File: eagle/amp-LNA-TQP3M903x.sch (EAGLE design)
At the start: 17 parts, among them J1 142-0701-851, J2 142-0701-851, U1 TQP3M903X

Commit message: Tune S band
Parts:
- added C7: 2.4p, oresat-rcl:C-EU0402-C-NOSILK
- added L2: 2.7n, oresat-rcl:L-US0402-C-NOSILK
- C5, C6: value ? -> 100p
- L1: value ? -> 4.3n
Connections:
- net RF_IN renamed N$6
- removed net N$32: C5.2, U1.IN
- new net N$4: C7.2, U1.IN
- new net N$5: C5.2, C7.1, L2.1
- net GND: now also L2.2
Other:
- note added: "L band - 1265MHz: L1 = ? L2 = ? C7 = ? Notes: C7 @ ? deg distance"
- note added: "S band - 2422MHz: L1 = 4.3n L2 = 2.7n C7 = 2.4p Notes: C7 @ 12 deg distance"
- note added: "UHF - 436.5MHz: L1 = ? L2 = ? C7 = ? Notes: C7 @ ? deg distance"
- note removed: "Allow for shunt"
- note removed: "Allow for shunt L"
- note removed: "Note: LC input/output networks require tuning"
- note removed: "UHF / L band / S band"
- moved on the sheet: C5, C6, J1
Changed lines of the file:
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@@
 </class>
 <class number="1" name="RF1" width="0" drill="0">
-<clearance class="1" value="0.4"/>
+<clearance class="1" value="0.5"/>
 </class>
 <class number="2" name="RF2" width="0" drill="0">
-<clearance class="2" value="0.6"/>
+<clearance class="2" value="0.4"/>
 </class>
 </classes>
@@
 <part name="GND27" library="supply1" library_urn="urn:adsk.eagle:library:371" deviceset="GND" device=""/>
 <part name="GND28" library="supply1" library_urn="urn:adsk.eagle:library:371" deviceset="GND" device=""/>
-<part name="C6" library="oresat-rcl" deviceset="C-EU" device="0402-C-NOSILK" value="?"/>
-<part name="C5" library="oresat-rcl" deviceset="C-EU" device="0402-C-NOSILK" value="?"/>
+<part name="C6" library="oresat-rcl" deviceset="C-EU" device="0402-C-NOSILK" value="100p"/>
+<part name="C5" library="oresat-rcl" deviceset="C-EU" device="0402-C-NOSILK" value="100p"/>
 <part name="GND29" library="supply1" library_urn="urn:adsk.eagle:library:371" deviceset="GND" device=""/>
 <part name="GND30" library="supply1" library_urn="urn:adsk.eagle:library:371" deviceset="GND" device=""/>
@@
 <part name="R5" library="oresat-rcl" deviceset="R-US_" device="0603-B-NOSILK" value="10k"/>
 <part name="GND3" library="supply1" library_urn="urn:adsk.eagle:library:371" deviceset="GND" device=""/>
-<part name="L1" library="oresat-rcl" deviceset="L-US" device="0603-C-NOSILK" value="?"/>
+<part name="L1" library="oresat-rcl" deviceset="L-US" device="0603-C-NOSILK" value="4.3n"/>
+<part name="C7" library="oresat-rcl" deviceset="C-EU" device="0402-C-NOSILK" value="2.4p"/>
+<part name="L2" library="oresat-rcl" deviceset="L-US" device="0402-C-NOSILK" value="2.7n"/>
+<part name="GND2" library="supply1" library_urn="urn:adsk.eagle:library:371" deviceset="GND" device=""/>
 </parts>
 <sheets>
@@
 <text x="176.53" y="26.67" size="5.08" layer="94">LNA: Qorvo TQP3M9035/6/7</text>
 <text x="265.43" y="6.35" size="3.81" layer="94">1</text>
-<text x="162.56" y="86.36" size="1.778" layer="97">Note: LC input/output networks require tuning</text>
 <text x="170.18" y="137.16" size="1.778" layer="97">Bias Resistor NOT Required</text>
-<text x="163.83" y="68.58" size="1.778" layer="97">UHF / L band / S band</text>
+<text x="173.99" y="81.28" size="1.778" layer="97" rot="MR180">S band - 2422MHz:
+L1 = 4.3n
+L2 = 2.7n
+C7 = 2.4p
+Notes:
+C7 @ 12 deg distance</text>
 <text x="95.25" y="74.93" size="1.778" layer="97">Shutdown (High)
 Enable (Low - Default)</text>
@@
 External</text>
 <text x="121.92" y="110.49" size="1.778" layer="97">Pad for input bias</text>
-<text x="102.87" y="99.06" size="1.778" layer="97">Allow for shunt L</text>
-<text x="182.88" y="99.06" size="1.778" layer="97">Allow for shunt</text>
+<text x="208.28" y="81.28" size="1.778" layer="97" rot="MR180">L band - 1265MHz:
+L1 = ?
+L2 = ?
+C7 = ?
+Notes:
+C7 @ ? deg distance</text>
+<text x="241.3" y="81.28" size="1.778" layer="97" rot="MR180">UHF - 436.5MHz:
+L1 = ?
+L2 = ?
+C7 = ?
+Notes:
+C7 @ ? deg distance</text>
 </plain>
 <instances>
@@
 <attribute name="VALUE" x="157.48" y="82.55" size="1.778" layer="96" rot="MR0"/>
 </instance>
-<instance part="C6" gate="CE" x="173.99" y="104.14" smashed="yes" rot="MR270">
-<attribute name="NAME" x="173.609" y="102.616" size="1.778" layer="95" rot="MR270"/>
-<attribute name="VALUE" x="178.689" y="102.616" size="1.778" layer="96" rot="MR270"/>
-</instance>
-<instance part="C5" gate="CE" x="119.38" y="104.14" smashed="yes" rot="R90">
-<attribute name="NAME" x="118.999" y="105.664" size="1.778" layer="95" rot="R90"/>
-<attribute name="VALUE" x="124.079" y="105.664" size="1.778" layer="96" rot="R90"/>
+<instance part="C6" gate="CE" x="182.88" y="104.14" smashed="yes" rot="MR270">
+<attribute name="NAME" x="182.499" y="102.616" size="1.778" layer="95" rot="MR270"/>
+<attribute name="VALUE" x="187.579" y="102.616" size="1.778" layer="96" rot="MR270"/>
+</instance>
+<instance part="C5" gate="CE" x="101.6" y="104.14" smashed="yes" rot="R90">
+<attribute name="NAME" x="101.219" y="105.664" size="1.778" layer="95" rot="R90"/>
+<attribute name="VALUE" x="106.299" y="105.664" size="1.778" layer="96" rot="R90"/>
 </instance>
 <instance part="GND29" gate="1" x="201.93" y="96.52" smashed="yes">
 <attribute name="VALUE" x="199.39" y="93.98" size="1.778" layer="96"/>
 </instance>
-<instance part="GND30" gate="1" x="99.06" y="96.52" smashed="yes" rot="MR0">
-<attribute name="VALUE" x="101.6" y="93.98" size="1.778" layer="96" rot="MR0"/>
+<instance part="GND30" gate="1" x="93.98" y="96.52" smashed="yes" rot="MR0">
+<attribute name="VALUE" x="96.52" y="93.98" size="1.778" layer="96" rot="MR0"/>
 </instance>
 <instance part="GND81" gate="1" x="200.66" y="114.3" smashed="yes">
@@
 <attribute name="VALUE" x="156.21" y="151.638" size="1.778" layer="96"/>
 </instance>
-<instance part="J1" gate="G$1" x="93.98" y="104.14" smashed="yes">
-<attribute name="NAME" x="91.44" y="99.06" size="1.778" layer="95"/>
-<attribute name="VALUE" x="85.09" y="106.68" size="1.778" layer="96"/>
+<instance part="J1" gate="G$1" x="88.9" y="104.14" smashed="yes">
+<attribute name="NAME" x="86.36" y="99.06" size="1.778" layer="95"/>
+<attribute name="VALUE" x="80.01" y="106.68" size="1.778" layer="96"/>
 </instance>
 <instance part="J2" gate="G$1" x="207.01" y="104.14" smashed="yes" rot="MR0">
@@
 <attribute name="NAME" x="163.83" y="116.84" size="1.778" layer="95"/>
 <attribute name="VALUE" x="168.91" y="116.84" size="1.778" layer="96"/>
+</instance>
+<instance part="C7" gate="CE" x="121.92" y="104.14" smashed="yes" rot="MR270">
+<attribute name="NAME" x="121.539" y="102.616" size="1.778" layer="95" rot="MR270"/>
+<attribute name="VALUE" x="126.619" y="102.616" size="1.778" layer="96" rot="MR270"/>
+</instance>
+<instance part="L2" gate="L" x="114.3" y="92.71" smashed="yes" rot="R270">
+<attribute name="NAME" x="110.49" y="93.98" size="1.778" layer="95"/>
+<attribute name="VALUE" x="115.57" y="93.98" size="1.778" layer="96"/>
+</instance>
+<instance part="GND2" gate="1" x="114.3" y="85.09" smashed="yes" rot="MR0">
+<attribute name="VALUE" x="116.84" y="82.55" size="1.778" layer="96" rot="MR0"/>
 </instance>
 </instances>
@@
 </segment>
 <segment>
-<wire x1="99.06" y1="101.6" x2="96.52" y2="101.6" width="0.1524" layer="91"/>
+<wire x1="93.98" y1="101.6" x2="91.44" y2="101.6" width="0.1524" layer="91"/>
 <pinref part="GND30" gate="1" pin="GND"/>
-<wire x1="99.06" y1="99.06" x2="99.06" y2="101.6" width="0.1524" layer="91"/>
+<wire x1="93.98" y1="99.06" x2="93.98" y2="101.6" width="0.1524" layer="91"/>
 <pinref part="J1" gate="G$1" pin="GND"/>
 </segment>
@@
 <wire x1="149.86" y1="71.12" x2="149.86" y2="69.85" width="0.1524" layer="91"/>
 </segment>
+<segment>
+<pinref part="L2" gate="L" pin="2"/>
+<pinref part="GND2" gate="1" pin="GND"/>
+</segment>
 </net>
 <net name="N$28" class="1">
@@
 <wire x1="167.64" y1="104.14" x2="167.64" y2="110.49" width="0.1524" layer="91"/>
 <pinref part="C6" gate="CE" pin="1"/>
-<wire x1="171.45" y1="104.14" x2="167.64" y2="104.14" width="0.1524" layer="91"/>
+<wire x1="180.34" y1="104.14" x2="167.64" y2="104.14" width="0.1524" layer="91"/>
 <junction x="167.64" y="104.14"/>
 <pinref part="L1" gate="L" pin="2"/>
 </segment>
 </net>
-<net name="N$32" class="1">
-<segment>
-<pinref part="C5" gate="CE" pin="2"/>
-<pinref part="U1" gate="G$1" pin="IN"/>
-<wire x1="124.46" y1="104.14" x2="137.16" y2="104.14" width="0.1524" layer="91"/>
-</segment>
-</net>
-<net name="RF_OUT" class="2">
+<net name="RF_OUT" class="1">
 <segment>
 <wire x1="199.39" y1="104.14" x2="204.47" y2="104.14" width="0.1524" layer="91"/>
 <pinref part="C6" gate="CE" pin="2"/>
-<wire x1="199.39" y1="104.14" x2="179.07" y2="104.14" width="0.1524" layer="91"/>
+<wire x1="199.39" y1="104.14" x2="187.96" y2="104.14" width="0.1524" layer="91"/>
 <pinref part="J2" gate="G$1" pin="RF"/>
-</segment>
-</net>
-<net name="RF_IN" class="2">
-<segment>
-<wire x1="101.6" y1="104.14" x2="96.52" y2="104.14" width="0.1524" layer="91"/>
-<wire x1="101.6" y1="104.14" x2="106.68" y2="104.14" width="0.1524" layer="91"/>
-<pinref part="C5" gate="CE" pin="1"/>
-<pinref part="J1" gate="G$1" pin="RF"/>
-<wire x1="106.68" y1="104.14" x2="116.84" y2="104.14" width="0.1524" layer="91"/>
 </segment>
 </net>
@@
 </segment>
 </net>
+<net name="N$4" class="1">
+<segment>
+<pinref part="C7" gate="CE" pin="2"/>
+<pinref part="U1" gate="G$1" pin="IN"/>
+<wire x1="127" y1="104.14" x2="137.16" y2="104.14" width="0.1524" layer="91"/>
+</segment>
+</net>
+<net name="N$5" class="1">
+<segment>
+<pinref part="C7" gate="CE" pin="1"/>
+<pinref part="C5" gate="CE" pin="2"/>
+<wire x1="119.38" y1="104.14" x2="114.3" y2="104.14" width="0.1524" layer="91"/>
+<pinref part="L2" gate="L" pin="1"/>
+<wire x1="114.3" y1="104.14" x2="106.68" y2="104.14" width="0.1524" layer="91"/>
+<wire x1="114.3" y1="100.33" x2="114.3" y2="104.14" width="0.1524" layer="91"/>
+<junction x="114.3" y="104.14"/>
+</segment>
+</net>
+<net name="N$6" class="1">
+<segment>
+<pinref part="C5" gate="CE" pin="1"/>
+<pinref part="J1" gate="G$1" pin="RF"/>
+<wire x1="99.06" y1="104.14" x2="91.44" y2="104.14" width="0.1524" layer="91"/>
+</segment>
+</net>

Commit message: Minor fixes
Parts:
- removed C7: 2.4p, oresat-rcl:C-EU0402-C-NOSILK
- C5: value 100p -> 2.4p
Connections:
- removed net N$5: C5.2, C7.1, L2.1
- removed net N$6: C5.1, J1.RF
- new net RF_IN: C5.1, J1.RF, L2.1
- net N$4: now also C5.2; no longer C7.2
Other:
- note added: "L band - 1265MHz: L1 = ? L2 = ? C7 = ? Notes: C5 @ ? deg distance"
- note added: "S band - 2422MHz: L1 = 4.3n L2 = 2.7n C7 = 2.4p Notes: C5 @ 12 deg distance Tuned for 3.3V"
- note added: "UHF - 436.5MHz: L1 = ? L2 = ? C7 = ? Notes: C5 @ ? deg distance"
- note removed: "L band - 1265MHz: L1 = ? L2 = ? C7 = ? Notes: C7 @ ? deg distance"
- note removed: "S band - 2422MHz: L1 = 4.3n L2 = 2.7n C7 = 2.4p Notes: C7 @ 12 deg distance"
- note removed: "UHF - 436.5MHz: L1 = ? L2 = ? C7 = ? Notes: C7 @ ? deg distance"
- moved on the sheet: C5
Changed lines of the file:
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@@
 </class>
 <class number="2" name="RF2" width="0" drill="0">
-<clearance class="2" value="0.4"/>
+<clearance class="2" value="0.8"/>
 </class>
 </classes>
@@
 <part name="GND28" library="supply1" library_urn="urn:adsk.eagle:library:371" deviceset="GND" device=""/>
 <part name="C6" library="oresat-rcl" deviceset="C-EU" device="0402-C-NOSILK" value="100p"/>
-<part name="C5" library="oresat-rcl" deviceset="C-EU" device="0402-C-NOSILK" value="100p"/>
 <part name="GND29" library="supply1" library_urn="urn:adsk.eagle:library:371" deviceset="GND" device=""/>
 <part name="GND30" library="supply1" library_urn="urn:adsk.eagle:library:371" deviceset="GND" device=""/>
@@
 <part name="GND3" library="supply1" library_urn="urn:adsk.eagle:library:371" deviceset="GND" device=""/>
 <part name="L1" library="oresat-rcl" deviceset="L-US" device="0603-C-NOSILK" value="4.3n"/>
-<part name="C7" library="oresat-rcl" deviceset="C-EU" device="0402-C-NOSILK" value="2.4p"/>
+<part name="C5" library="oresat-rcl" deviceset="C-EU" device="0402-C-NOSILK" value="2.4p"/>
 <part name="L2" library="oresat-rcl" deviceset="L-US" device="0402-C-NOSILK" value="2.7n"/>
 <part name="GND2" library="supply1" library_urn="urn:adsk.eagle:library:371" deviceset="GND" device=""/>
@@
 C7 = 2.4p
 Notes:
-C7 @ 12 deg distance</text>
+C5 @ 12 deg distance
+Tuned for 3.3V</text>
 <text x="95.25" y="74.93" size="1.778" layer="97">Shutdown (High)
 Enable (Low - Default)</text>
@@
 C7 = ?
 Notes:
-C7 @ ? deg distance</text>
+C5 @ ? deg distance</text>
 <text x="241.3" y="81.28" size="1.778" layer="97" rot="MR180">UHF - 436.5MHz:
 L1 = ?
@@
 C7 = ?
 Notes:
-C7 @ ? deg distance</text>
+C5 @ ? deg distance</text>
 </plain>
 <instances>
@@
 <attribute name="VALUE" x="187.579" y="102.616" size="1.778" layer="96" rot="MR270"/>
 </instance>
-<instance part="C5" gate="CE" x="101.6" y="104.14" smashed="yes" rot="R90">
-<attribute name="NAME" x="101.219" y="105.664" size="1.778" layer="95" rot="R90"/>
-<attribute name="VALUE" x="106.299" y="105.664" size="1.778" layer="96" rot="R90"/>
-</instance>
 <instance part="GND29" gate="1" x="201.93" y="96.52" smashed="yes">
 <attribute name="VALUE" x="199.39" y="93.98" size="1.778" layer="96"/>
@@
 <attribute name="VALUE" x="168.91" y="116.84" size="1.778" layer="96"/>
 </instance>
-<instance part="C7" gate="CE" x="121.92" y="104.14" smashed="yes" rot="MR270">
+<instance part="C5" gate="CE" x="121.92" y="104.14" smashed="yes" rot="MR270">
 <attribute name="NAME" x="121.539" y="102.616" size="1.778" layer="95" rot="MR270"/>
 <attribute name="VALUE" x="126.619" y="102.616" size="1.778" layer="96" rot="MR270"/>
@@
 </segment>
 </net>
-<net name="RF_OUT" class="1">
+<net name="RF_OUT" class="2">
 <segment>
 <wire x1="199.39" y1="104.14" x2="204.47" y2="104.14" width="0.1524" layer="91"/>
@@
 <net name="N$4" class="1">
 <segment>
-<pinref part="C7" gate="CE" pin="2"/>
+<pinref part="C5" gate="CE" pin="2"/>
 <pinref part="U1" gate="G$1" pin="IN"/>
 <wire x1="127" y1="104.14" x2="137.16" y2="104.14" width="0.1524" layer="91"/>
 </segment>
 </net>
-<net name="N$5" class="1">
-<segment>
-<pinref part="C7" gate="CE" pin="1"/>
-<pinref part="C5" gate="CE" pin="2"/>
+<net name="RF_IN" class="2">
+<segment>
+<pinref part="C5" gate="CE" pin="1"/>
 <wire x1="119.38" y1="104.14" x2="114.3" y2="104.14" width="0.1524" layer="91"/>
 <pinref part="L2" gate="L" pin="1"/>
-<wire x1="114.3" y1="104.14" x2="106.68" y2="104.14" width="0.1524" layer="91"/>
 <wire x1="114.3" y1="100.33" x2="114.3" y2="104.14" width="0.1524" layer="91"/>
+<pinref part="J1" gate="G$1" pin="RF"/>
+<wire x1="91.44" y1="104.14" x2="114.3" y2="104.14" width="0.1524" layer="91"/>
 <junction x="114.3" y="104.14"/>
-</segment>
-</net>
-<net name="N$6" class="1">
-<segment>
-<pinref part="C5" gate="CE" pin="1"/>
-<pinref part="J1" gate="G$1" pin="RF"/>
-<wire x1="99.06" y1="104.14" x2="91.44" y2="104.14" width="0.1524" layer="91"/>
 </segment>
 </net>
@@
 </sheet>
 </sheets>
+<errors>
+</errors>
 </schematic>
 </drawing>

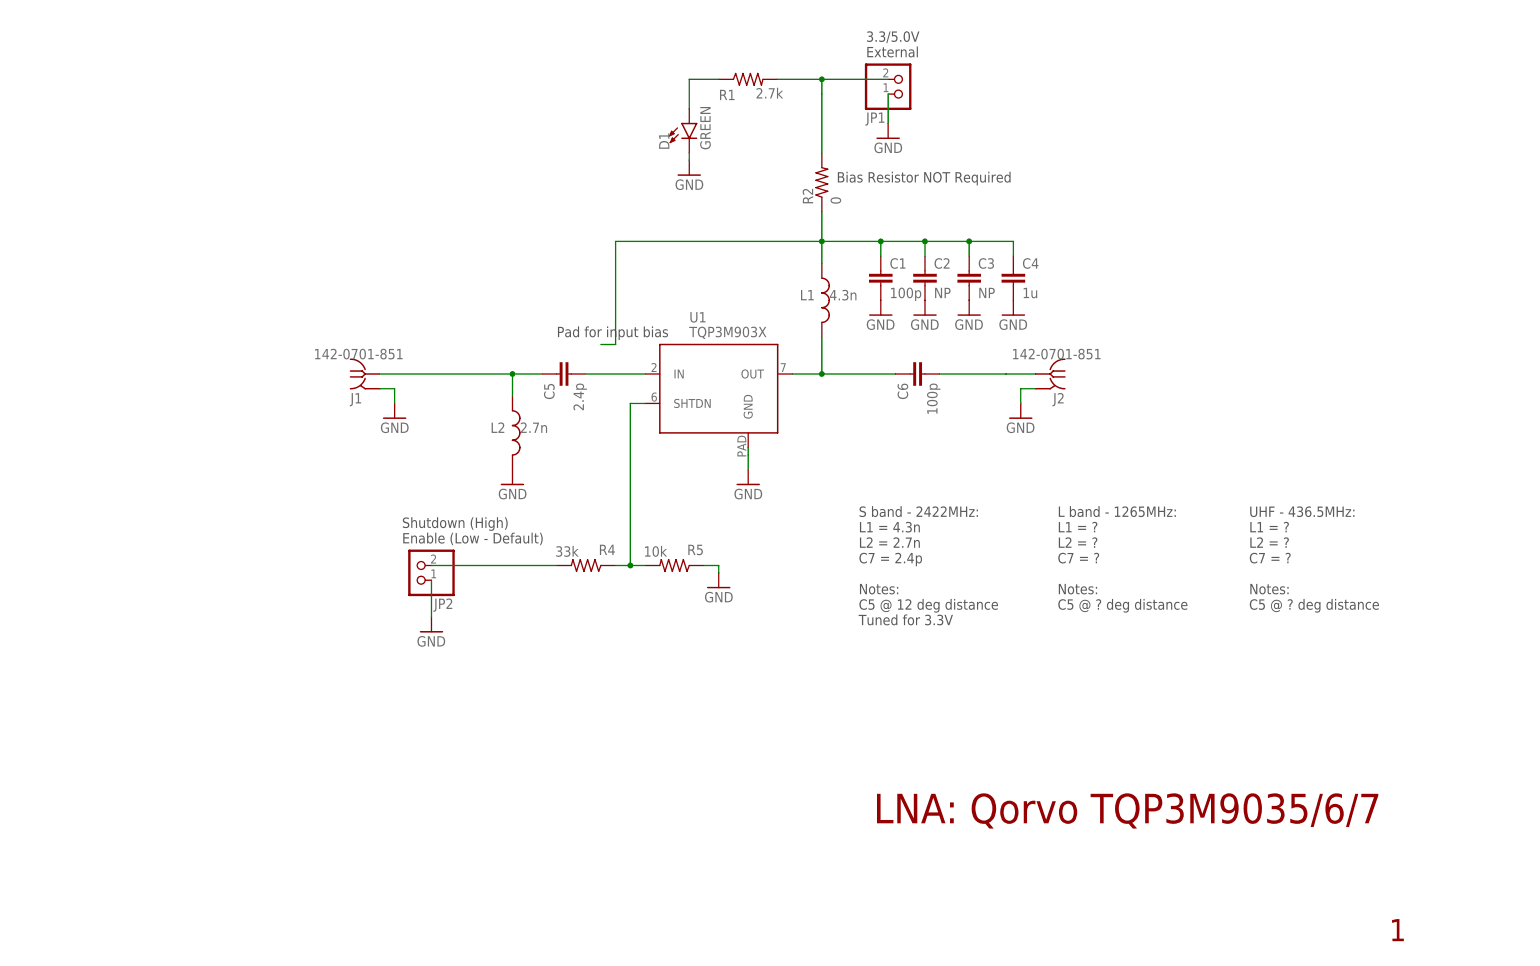
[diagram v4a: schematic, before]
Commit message: Adjust S band matching and add RF component MFG PNs
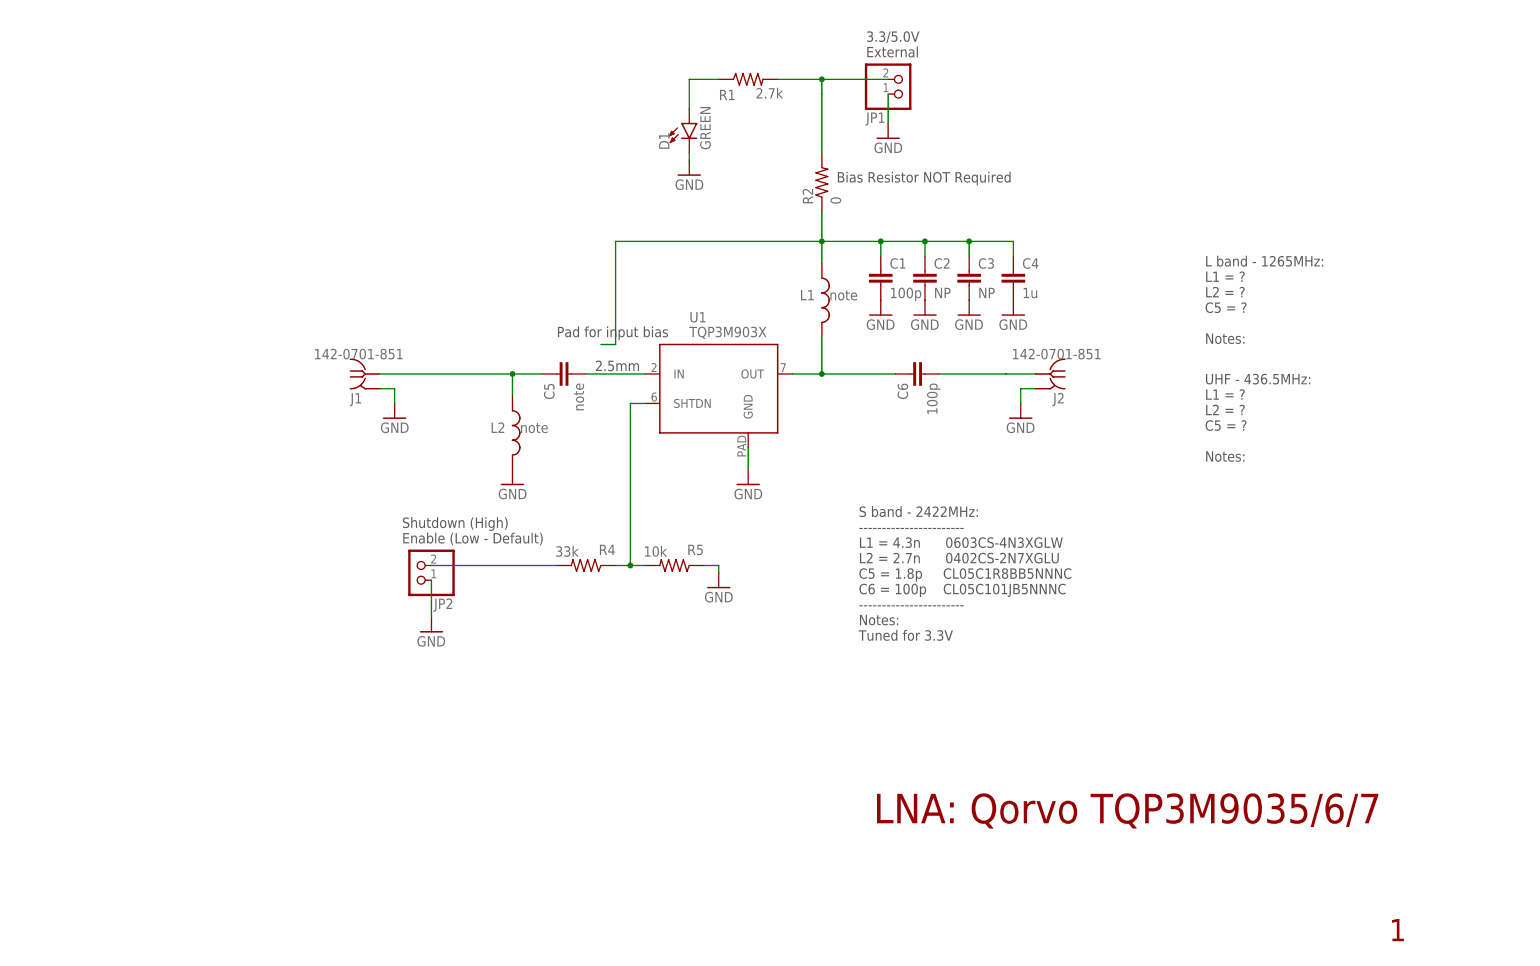
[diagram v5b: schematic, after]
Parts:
- C5: value 2.4p -> note
- L1: value 4.3n -> note
- L2: value 2.7n -> note
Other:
- note added: "2.5mm"
- note added: "L band - 1265MHz: L1 = ? L2 = ? C5 = ? Notes:"
- note added: "S band - 2422MHz: ----------------------- L1 = 4.3n 0603CS-4N3XGLW L2 = 2.7n 0402CS-2N7XGLU C5 = 1.8p CL05C1R8BB5NNNC C6 = 100p CL05C101JB5NNNC ----------------------- Notes: Tuned for 3.3V"
- note added: "UHF - 436.5MHz: L1 = ? L2 = ? C5 = ? Notes:"
- note removed: "L band - 1265MHz: L1 = ? L2 = ? C7 = ? Notes: C5 @ ? deg distance"
- note removed: "S band - 2422MHz: L1 = 4.3n L2 = 2.7n C7 = 2.4p Notes: C5 @ 12 deg distance Tuned for 3.3V"
- note removed: "UHF - 436.5MHz: L1 = ? L2 = ? C7 = ? Notes: C5 @ ? deg distance"
